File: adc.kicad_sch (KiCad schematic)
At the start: 22 parts, among them U6 TPS7B92050DBVR, U7 ADS7253

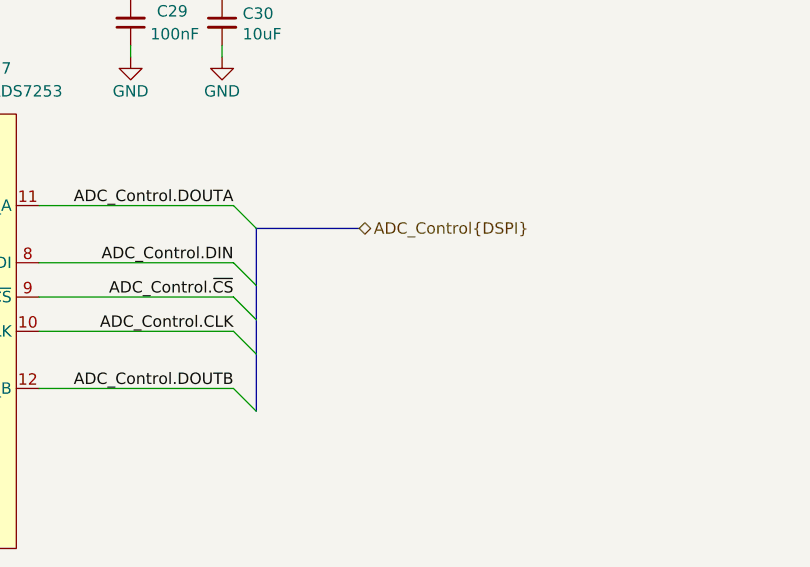
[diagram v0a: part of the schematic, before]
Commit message: Finished Board Layout
Schematic Changes
- Removed some testpoints
- Fixed Lib issues
- moved around FMC pinout

Layout
- routed all traces
- routed RF traces using Controlled Impedance in mind
- ERC/DRC free
- All silkscreen is arranged

Still to do
- finish net-classes for controlled traces
- create arc traces for diff CLK lines
- small tweaks to improve RF performance
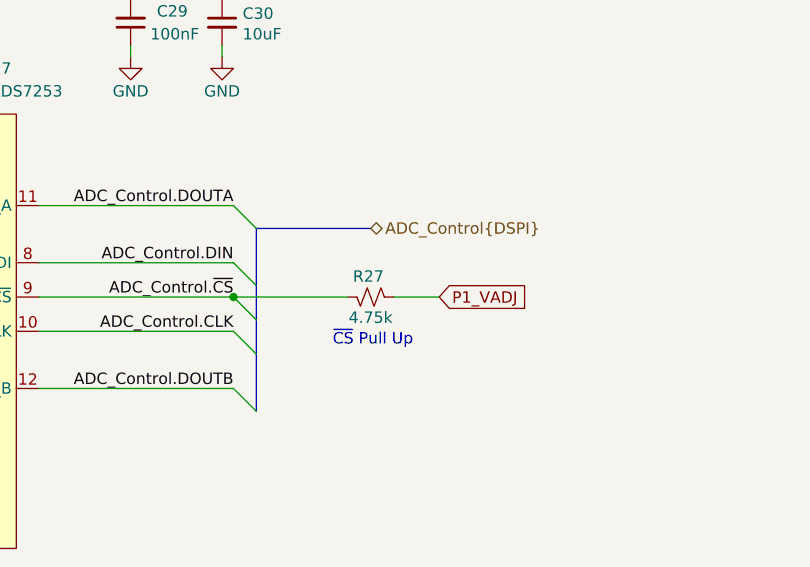
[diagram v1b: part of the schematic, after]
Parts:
- added R27: 4.75k, Resistor_SMD:R_0603_1608Metric, symbol Device:R_Small_US
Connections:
- net ADC_Control.~{CS}: now also R27.1
- net P1_VADJ: now also R27.2
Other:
- note added: "~{CS} Pull Up"
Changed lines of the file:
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@@
+		)
+	)
+	(text "~{CS} Pull Up"
+		(exclude_from_sim no)
+		(at 195.834 107.696 0)
+		(effects
+			(font
+				(size 1.27 1.27)
+			)
 		)
 	)
@@
 	)
 	(junction
+		(at 180.34 102.87)
+		(diameter 0)
+		(color 0 0 0 0)
+	)
+	(junction
 		(at 168.91 67.31)
 		(diameter 0)
@@
 	(wire
 		(pts
+			(xy 180.34 102.87) (xy 193.04 102.87)
+		)
+		(stroke
+			(width 0)
+			(type default)
+		)
+	)
+	(wire
+		(pts
 			(xy 179.07 67.31) (xy 189.23 67.31)
 		)
@@
 	(bus
 		(pts
-			(xy 182.88 95.25) (xy 194.31 95.25)
+			(xy 182.88 95.25) (xy 195.58 95.25)
 		)
 		(stroke
@@
 		(pts
 			(xy 78.74 68.58) (xy 78.74 69.85)
+		)
+		(stroke
+			(width 0)
+			(type default)
+		)
+	)
+	(wire
+		(pts
+			(xy 198.12 102.87) (xy 203.2 102.87)
 		)
 		(stroke
@@
 			)
 			(justify right bottom)
+		)
+	)
+	(global_label "P1_VADJ"
+		(shape input)
+		(at 203.2 102.87 0)
+		(fields_autoplaced yes)
+		(effects
+			(font
+				(size 1.27 1.27)
+			)
+			(justify left)
+		)
+		(property "Intersheetrefs" "${INTERSHEET_REFS}"
+			(at 214.0471 102.87 0)
+			(effects
+				(font
+					(size 1.27 1.27)
+				)
+				(justify left)
+			)
 		)
 	)
@@
 	(hierarchical_label "ADC_Control{DSPI}"
 		(shape bidirectional)
-		(at 194.31 95.25 0)
+		(at 195.58 95.25 0)
 		(effects
 			(font
@@
 					(unit 1)
 				)
+			)
+		)
+	)
+	(symbol
+		(lib_id "Device:R_Small_US")
+		(at 195.58 102.87 90)
+		(mirror x)
+		(unit 1)
+		(exclude_from_sim no)
+		(in_bom yes)
+		(on_board yes)
+		(dnp no)
+		(property "Reference" "R27"
+			(at 195.326 100.584 90)
+			(effects
+				(font
+					(size 1.27 1.27)
+				)
+			)
+		)
+		(property "Value" "4.75k"
+			(at 195.58 105.156 90)
+			(effects
+				(font
+					(size 1.27 1.27)
+				)
+			)
+		)
+		(property "Footprint" "Resistor_SMD:R_0603_1608Metric"
+			(at 195.58 102.87 0)
+			(effects
+				(font
+					(size 1.27 1.27)
+				)
+				(hide yes)
+			)
+		)
+		(property "Datasheet" "~"
+			(at 195.58 102.87 0)
+			(effects
+				(font
+					(size 1.27 1.27)
+				)
+				(hide yes)
+			)
+		)
+		(property "Description" "RES 4.75K OHM 1% 1/10W 0603"
+			(at 195.58 102.87 0)
+			(effects
+				(font
+					(size 1.27 1.27)
+				)
+				(hide yes)
+			)
+		)
+		(property "MPN" "RC0603FR-134K75L"
+			(at 195.58 102.87 0)
+			(effects
+				(font
+					(size 1.27 1.27)
+				)
+				(hide yes)
+			)
+		)
+		(property "Manufacturer" "Yageo "
+			(at 195.58 102.87 0)
+			(effects
+				(font
+					(size 1.27 1.27)
+				)
+				(hide yes)
+			)
+		)
+		(property "Supplier" "Digikey"
+			(at 195.58 102.87 0)
+			(effects
+				(font
+					(size 1.27 1.27)
+				)
+				(hide yes)
+			)
+		)
+		(property "Supplier Part Number" "311-4.42KHRCT-ND"
+			(at 195.58 102.87 0)
+			(effects
+				(font
+					(size 1.27 1.27)
+				)
+				(hide yes)
+			)
+		)
+		(pin "1"
+		)
+		(pin "2"
+		)
+		(instances
+			(project "rf-input-fmc"
+				(path "/1719e569-47c8-4fa0-8523-9c9686ef0dba/d098b615-7cba-44eb-be59-7a71f2f48c2b"
+					(reference "R27")
+					(unit 1)
+				)

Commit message: Tweaks to Layout/ fixed project errors
-Adjusted Testpoints by changing the value field to visible on the silkscreen layer.
- Fixed DRC and ERC issues

Known to do:
- run rounded traces
- determine neg/gnd pin of J20 (do we want to float but diff? SE?)
- determine/implement best practice grounding for mounting holes?
- Additional RF trace tweaking
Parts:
- TP16: value TestPoint -> ADC_DOUTA
- TP17: value TestPoint -> ADC_DIN
- TP18: value TestPoint -> ADC_CS
- TP19: value TestPoint -> ADC_CLK
- TP20: value TestPoint -> ADC_DOUTB
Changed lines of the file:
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@@
 	)
 	(junction
+		(at 143.51 58.42)
+		(diameter 0)
+		(color 0 0 0 0)
+	)
+	(junction
 		(at 100.33 91.44)
 		(diameter 0)
@@
 			)
 		)
-		(property "Value" "TestPoint"
+		(property "Value" "ADC_CLK"
 			(at 256.54 27.9399 90)
 			(effects
@@
 	)
 	(symbol
+		(lib_id "power:PWR_FLAG")
+		(at 143.51 58.42 270)
+		(mirror x)
+		(unit 1)
+		(exclude_from_sim no)
+		(in_bom yes)
+		(on_board yes)
+		(dnp no)
+		(fields_autoplaced yes)
+		(property "Reference" "#FLG04"
+			(at 145.415 58.42 0)
+			(effects
+				(font
+					(size 1.27 1.27)
+				)
+				(hide yes)
+			)
+		)
+		(property "Value" "PWR_FLAG"
+			(at 147.32 58.4199 90)
+			(effects
+				(font
+					(size 1.27 1.27)
+				)
+				(justify left)
+			)
+		)
+		(property "Footprint" ""
+			(at 143.51 58.42 0)
+			(effects
+				(font
+					(size 1.27 1.27)
+				)
+				(hide yes)
+			)
+		)
+		(property "Datasheet" "~"
+			(at 143.51 58.42 0)
+			(effects
+				(font
+					(size 1.27 1.27)
+				)
+				(hide yes)
+			)
+		)
+		(property "Description" "Special symbol for telling ERC where power comes from"
+			(at 143.51 58.42 0)
+			(effects
+				(font
+					(size 1.27 1.27)
+				)
+				(hide yes)
+			)
+		)
+		(pin "1"
+		)
+		(instances
+			(project "rf-input-fmc"
+				(path "/1719e569-47c8-4fa0-8523-9c9686ef0dba/d098b615-7cba-44eb-be59-7a71f2f48c2b"
+					(reference "#FLG04")
+					(unit 1)
+				)
+			)
+		)
+	)
+	(symbol
 		(lib_id "Connector:TestPoint")
 		(at 251.46 21.59 270)
@@
 			)
 		)
-		(property "Value" "TestPoint"
+		(property "Value" "ADC_DIN"
 			(at 256.54 22.8599 90)
 			(effects
@@
 			)
 		)
-		(property "Value" "TestPoint"
+		(property "Value" "ADC_DOUTA"
 			(at 256.54 20.3199 90)
 			(effects
@@
 			)
 		)
-		(property "Value" "TestPoint"
+		(property "Value" "ADC_DOUTB"
 			(at 256.54 30.4799 90)
 			(effects
@@
 			)
 		)
-		(property "Value" "TestPoint"
+		(property "Value" "ADC_CS"
 			(at 256.54 25.3999 90)
 			(effects

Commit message: quiet some kibot complaints
space at end of property value
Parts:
- R27, R5, R6, R7, R8: Manufacturer Yageo -> Yageo
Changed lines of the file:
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@@
 			)
 		)
-		(property "Manufacturer" "Yageo "
+		(property "Manufacturer" "Yageo"
 			(at 195.58 102.87 0)
 			(effects
@@
 			)
 		)
-		(property "Manufacturer" "Yageo "
+		(property "Manufacturer" "Yageo"
 			(at 91.44 97.79 0)
 			(effects
@@
 			)
 		)
-		(property "Manufacturer" "Yageo "
+		(property "Manufacturer" "Yageo"
 			(at 85.09 114.3 0)
 			(effects
@@
 			)
 		)
-		(property "Manufacturer" "Yageo "
+		(property "Manufacturer" "Yageo"
 			(at 85.09 91.44 0)
 			(effects
@@
 			)
 		)
-		(property "Manufacturer" "Yageo "
+		(property "Manufacturer" "Yageo"
 			(at 91.44 120.65 0)
 			(effects

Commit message: Updated Supplier part numbers
Updated Supplier part number for parts with incorrect or missing info
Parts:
- R27: Supplier Part Number 311-4.42KHRCT-ND -> 13-RC0603FR-134K75LCT-ND
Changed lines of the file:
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@@
 			)
 		)
-		(property "Supplier Part Number" "311-4.42KHRCT-ND"
+		(property "Supplier Part Number" "13-RC0603FR-134K75LCT-ND"
 			(at 195.58 102.87 0)
 			(effects

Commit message: Prototype Production Ready
- Removed Supplier and Supplier Part Numbers for project
- Changed Kibot to not out Supplier and Supplier Part Numbers for project
- Changed a few ignored ERC/DRC testing to warnings, and found no additional issues
- project is ready for production
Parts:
- C23, C28, C29: Supplier Digikey -> (none); Supplier Part Number 490-14514-1-ND -> (none)
- C24: Supplier Digikey -> (none); Supplier Part Number 490-7203-1-ND -> (none)
- C25, C26, C27, C30: Supplier Digikey -> (none); Supplier Part Number 490-13248-1-ND -> (none)
- C36, C37: Supplier Digikey -> (none); Supplier Part Number 445-174557-1-ND -> (none)
- R21: Supplier Digikey -> (none); Supplier Part Number P0.0ACT-ND -> (none)
- R27: Supplier Digikey -> (none); Supplier Part Number 13-RC0603FR-134K75LCT-ND -> (none)
- R5, R6: Supplier Digikey -> (none); Supplier Part Number 311-3.65KHRCT-ND -> (none)
- R7, R8: Supplier Digikey -> (none); Supplier Part Number 311-11.5KHRCT-ND -> (none)
- U6: Supplier Digikey -> (none); Supplier Part Number 296-TPS7B92050DBVRCT-ND -> (none)
- U7: Supplier Digikey -> (none); Supplier Part Number 296-38482-1-ND -> (none)

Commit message: Changes to Based on Pre-Production Run
- Added FPGA control for digital input buffer's OE pin with pull up
- Grounded ref caps on ADC properly
- Swapped pins 5&6 on U7 (polarity fix)
- Fixed naming of CLK inputs to be  "CLK1" / "CLK2" to be clk0 & clk1 inputs on LMK
    - Changed "J" tag to be digital IO only "J1 - J16"
- Mounting Holes changed 3.0mm to match with Marble
- Added 50ohm non-populated resistors in on digital inputs

- Changed labeling of ADC inputs in schematic (no copper changes)
- Changed labeling/assignment of digital inputs on the FMC connector (almost no copper changes)
	- now J1 = Dinput1 ... J15= Dinput16; J16 = PPS (PPS has unchanged mapping)
- Swapped h37 and g37 pin assignments (new D15 &D14)
	- for better compatibility with new FMC template

These changes were covered by moving to the new FMC template:
- Add heartbeat LED
- Add SN on both sides
- Move SN and logo to template side of board
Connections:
- net GND: now also C26.2, C27.2, U7.2 (REFGND_A), U7.3 (REFGND_B), U7.5 (AINB_N); no longer U7.6 (AINB_P)
- net at C37.2, R6.2, R8.2: now also U7.6 (AINB_P); no longer U7.5 (AINB_N)
- net RF_Level_1 renamed RF_Level_CLK2
- net RF_Level_2 renamed RF_Level_CLK1
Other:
- moved on the sheet: C26, C27, C37, R6, R8

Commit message: Updates based on Review
-Added Missing "PG_C2M" label
-Added heartbeat signal to fmc (was missing on previous commit)
-Changed all vias to 0.6mm with 0.3mm hole
	-Adjusted one via near pin7 of U7 to accommodate this change
-Changed traces around U4 to R25 to keep trace straight
-Added GND via at pin5 of U7 & connected all GND pins of U7 to PAD
-Moved R9 near J16 connector
-Changed name of board on silkscreen to "Clock Input FMC" project/file name changes will come in later commits.
-Standardized "J*" labels to all be consistent
-Swapped FMC pins for Din14 & Din15. This undoes some complications in the last commit with pin swaps
-Removed net references to "P1_" in net names
-Adjusted plane layers keepout and min width to be more consistent
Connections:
- net RF_Level_CLK1: now also R5.1; no longer R6.1
- net RF_Level_CLK2: now also R6.1; no longer R5.1
- net P1_12P0V renamed 12P0V
- net P1_VADJ renamed VADJ
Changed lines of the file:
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@@
 		)
 	)
-	(global_label "P1_VADJ"
+	(global_label "VADJ"
 		(shape input)
 		(at 203.2 102.87 0)
@@
 		)
 		(property "Intersheetrefs" "${INTERSHEET_REFS}"
-			(at 214.0471 102.87 0)
+			(at 210.6 102.87 0)
 			(effects
 				(font
@@
 		)
 	)
-	(global_label "P1_12P0V"
+	(global_label "12P0V"
 		(shape input)
 		(at 27.94 58.42 180)
@@
 		)
 		(property "Intersheetrefs" "${INTERSHEET_REFS}"
-			(at 15.5206 58.42 0)
+			(at 18.9677 58.42 0)
 			(effects
 				(font
@@
 		)
 	)
-	(global_label "P1_VADJ"
+	(global_label "VADJ"
 		(shape input)
 		(at 189.23 67.31 0)
@@
 		)
 		(property "Intersheetrefs" "${INTERSHEET_REFS}"
-			(at 200.0771 67.31 0)
+			(at 196.63 67.31 0)
 			(effects
 				(font
@@
 	(hierarchical_label "RF_Level_CLK1"
 		(shape input)
-		(at 78.74 111.76 180)
+		(at 78.74 91.44 180)
 		(effects
 			(font
@@
 	(hierarchical_label "RF_Level_CLK2"
 		(shape input)
-		(at 78.74 91.44 180)
+		(at 78.74 111.76 180)
 		(effects
 			(font

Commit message: Changed Title Blocks to Version 1.0
- changed title blocks
- changed silkscreen to add version number
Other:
- title: RF Input FMC Board -> Clock Input FMC Board
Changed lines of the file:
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@@
 	(paper "USLetter")
 	(title_block
-		(title "RF Input FMC Board")
-		(date "2025-10-16")
-		(rev "0.2")
+		(title "Clock Input FMC Board")
+		(date "2026-05-20")
+		(rev "1.0")
 		(company "SPDX-FileCopyrightText: 2025 Osprey DCS")
 		(comment 1 "SPDX-License-Identifier: CERN-OHL-S-2.0+")
